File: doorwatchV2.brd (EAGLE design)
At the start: 160 x 100 mm, 40 parts, among them IC2 MAX3232CPE, K1 FINDER-43.61, Q1 IRLZ44Z, T1 BC847, T2 BC847, T3 BC847, T4 BC847, X1 MKDSN1,5/2-5,08, X2 D-SUB9-H2M09RA, X3 MKDSN1,5/2-5,08

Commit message: first rough layout of components
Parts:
- moved Q1 209.2 mm to (149.9, 63.5), turned to 90 degrees
- moved X3 198.8 mm to (154.9, 94.0), turned to 90 degrees
- moved X1 181.5 mm to (154.9, 80.0), turned to 90 degrees
- moved K1 178.9 mm to (143.5, 91.4), turned to 90 degrees
- moved T3 176.9 mm to (99.1, 72.4)
- moved R10 172.7 mm to (149.9, 81.3), turned to 270 degrees
- moved R5 163.2 mm to (83.8, 64.8), turned to 90 degrees
- moved R1 157.6 mm to (83.8, 72.4), turned to 90 degrees
- moved R7 152.6 mm to (94.0, 71.1)
- moved R3 147.9 mm to (94.0, 66.0)
- moved OK1 146.3 mm to (85.1, 69.8), turned to 270 degrees
- moved T2 134.8 mm to (64.8, 68.6), turned to 270 degrees
- moved R9 127.4 mm to (58.4, 68.6), turned to 180 degrees
- moved T1 127.1 mm to (64.8, 64.8), turned to 270 degrees
- moved R8 122.6 mm to (58.4, 66.0), turned to 180 degrees
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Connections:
- net GND: now also LED4.C; no longer R11.2
- net N$28: now also R11.1; no longer LED4.A
- net N$29: now also LED4.A, R11.2; no longer LED4.C, R11.1

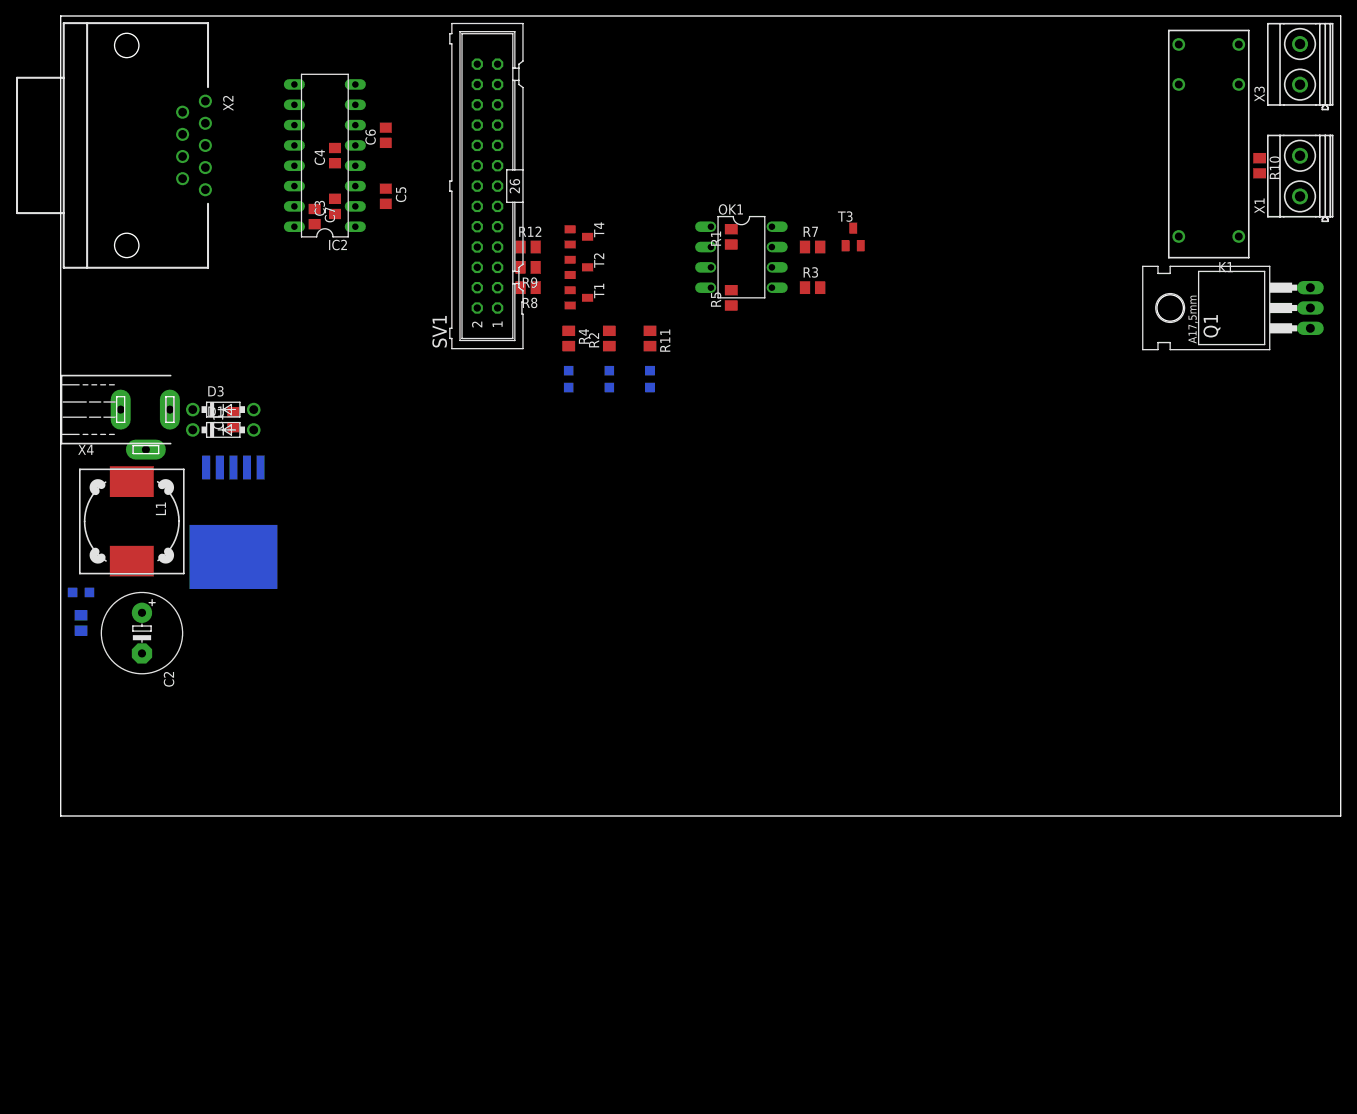
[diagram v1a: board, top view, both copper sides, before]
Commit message: added mounting-holes to schematic
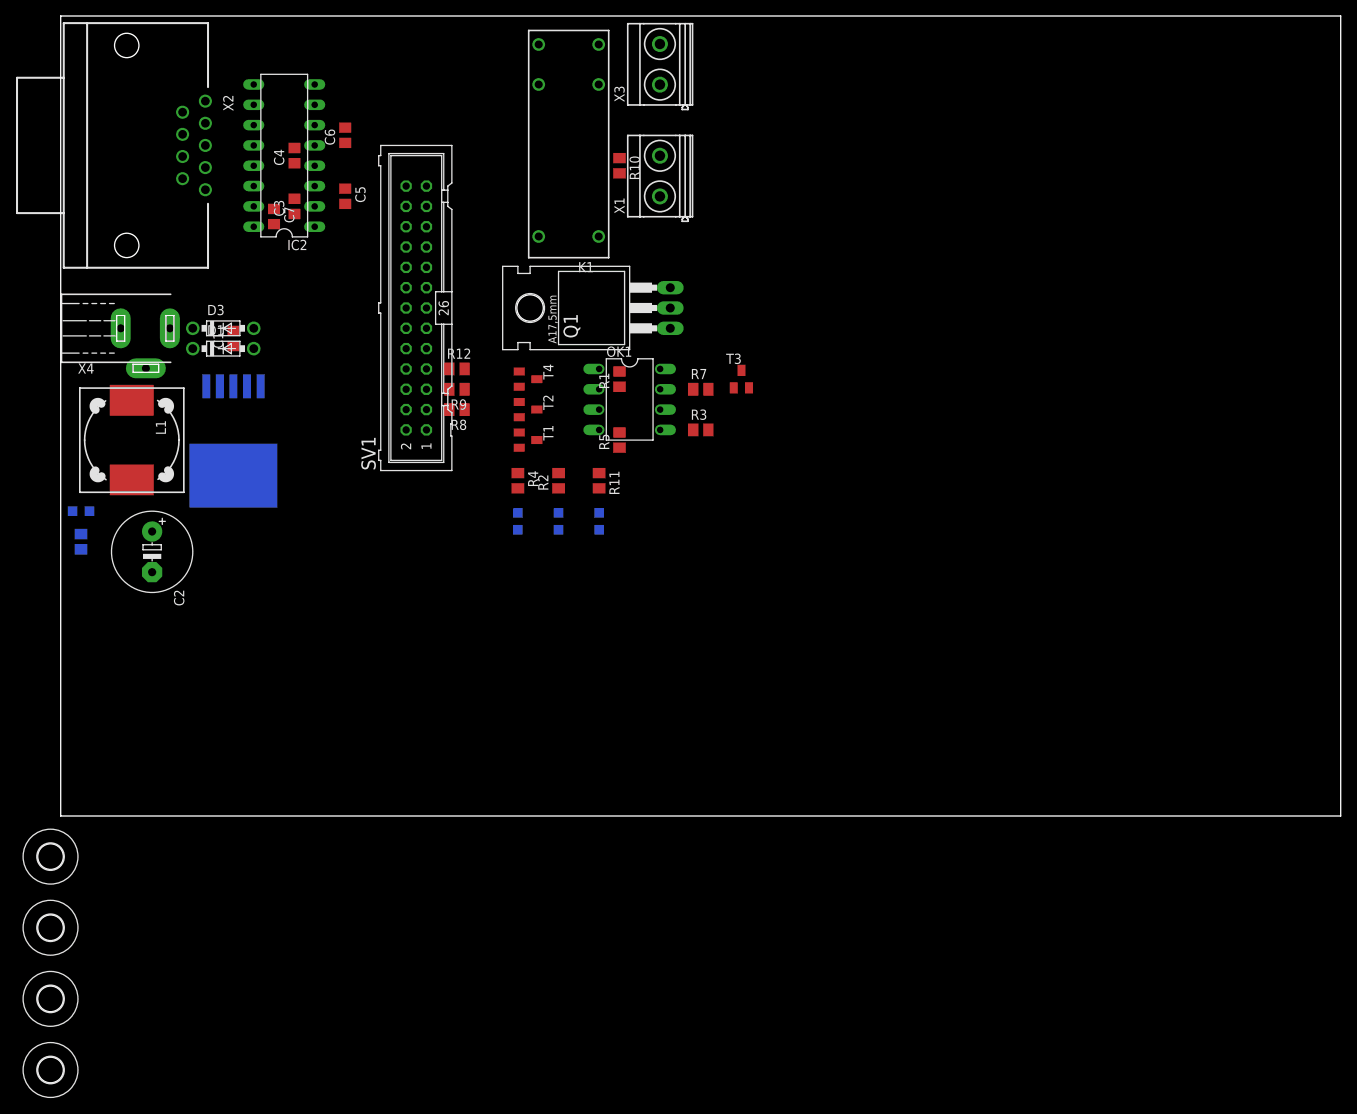
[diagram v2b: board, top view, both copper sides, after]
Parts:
- added H1, H2, H3, H4: MOUNT-HOLE3.2, holes:3,2
- moved Q1 80.0 mm to (69.8, 63.5)
- moved R10 80.0 mm to (69.8, 81.3)
- moved K1 80.0 mm to (63.5, 91.4)
- moved X1 80.0 mm to (74.9, 80.0)
- moved X3 80.0 mm to (74.9, 94.0)
- moved R3 22.6 mm to (80.0, 48.3)
- moved R1 22.6 mm to (69.8, 54.6)
- moved R7 22.6 mm to (80.0, 53.3)
- moved T3 22.6 mm to (85.1, 54.6)
- moved OK1 22.6 mm to (71.1, 52.1)
- moved R5 22.6 mm to (69.8, 47.0)
- moved LED1 18.9 mm to (57.1, 36.8)
- moved LED2 18.9 mm to (62.2, 36.8)
- moved LED4 18.9 mm to (67.3, 36.8)
- moved R11 18.9 mm to (67.3, 41.9)
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
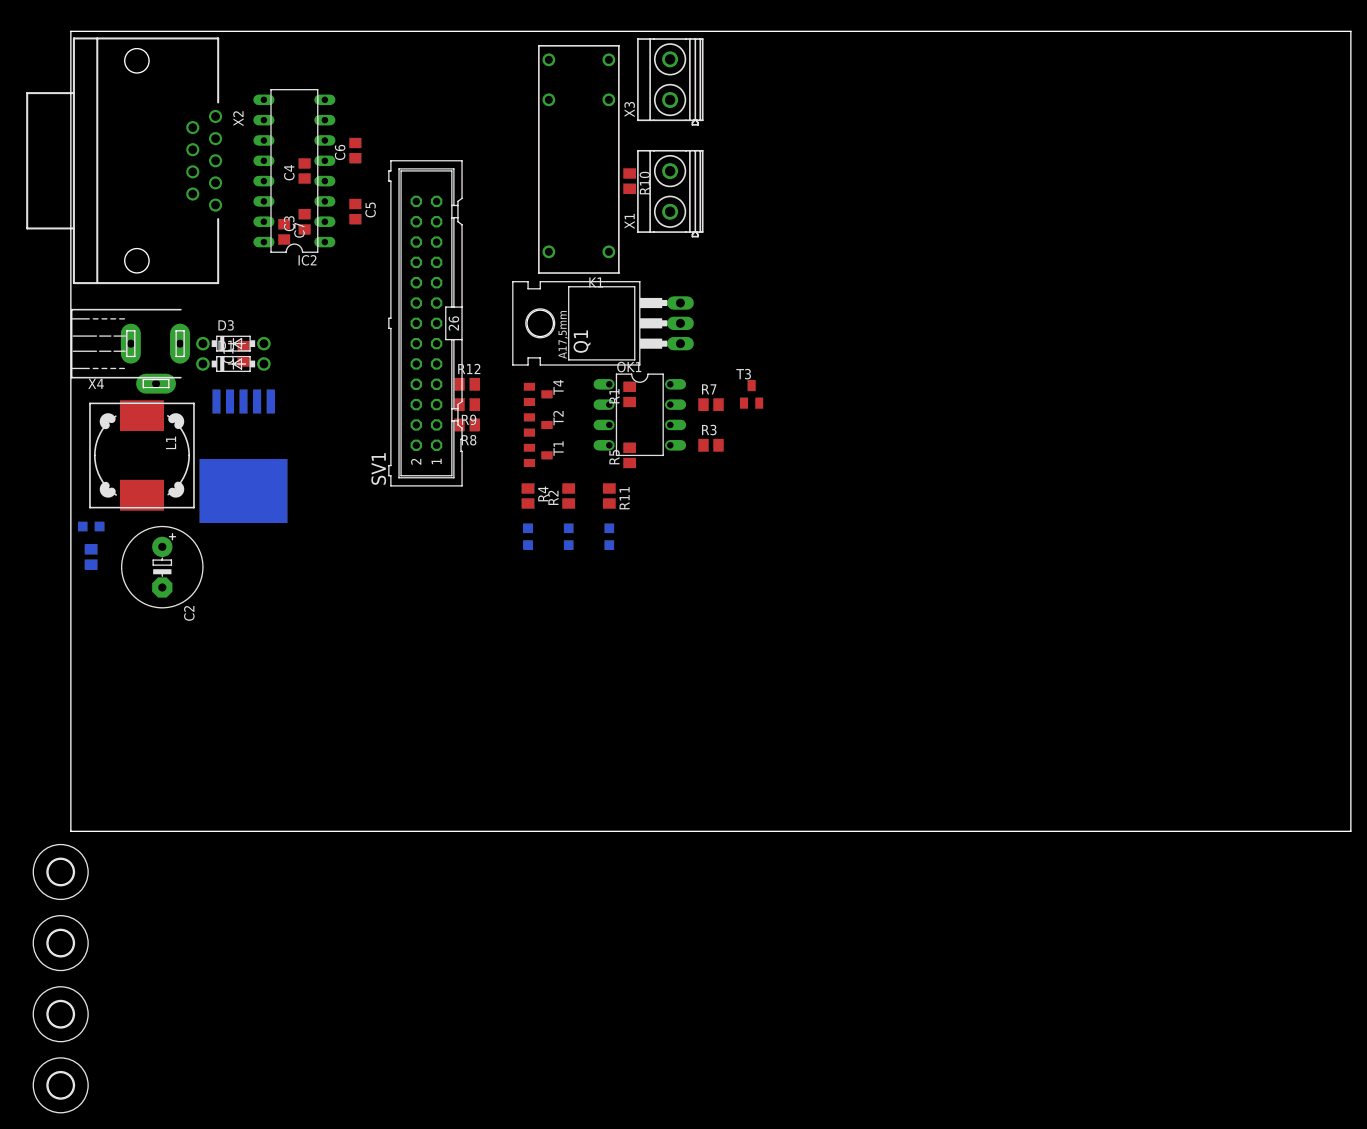
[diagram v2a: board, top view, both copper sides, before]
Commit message: first version of finished layout added white-print layers and adjusted it. adapted the trace width of higher current traces
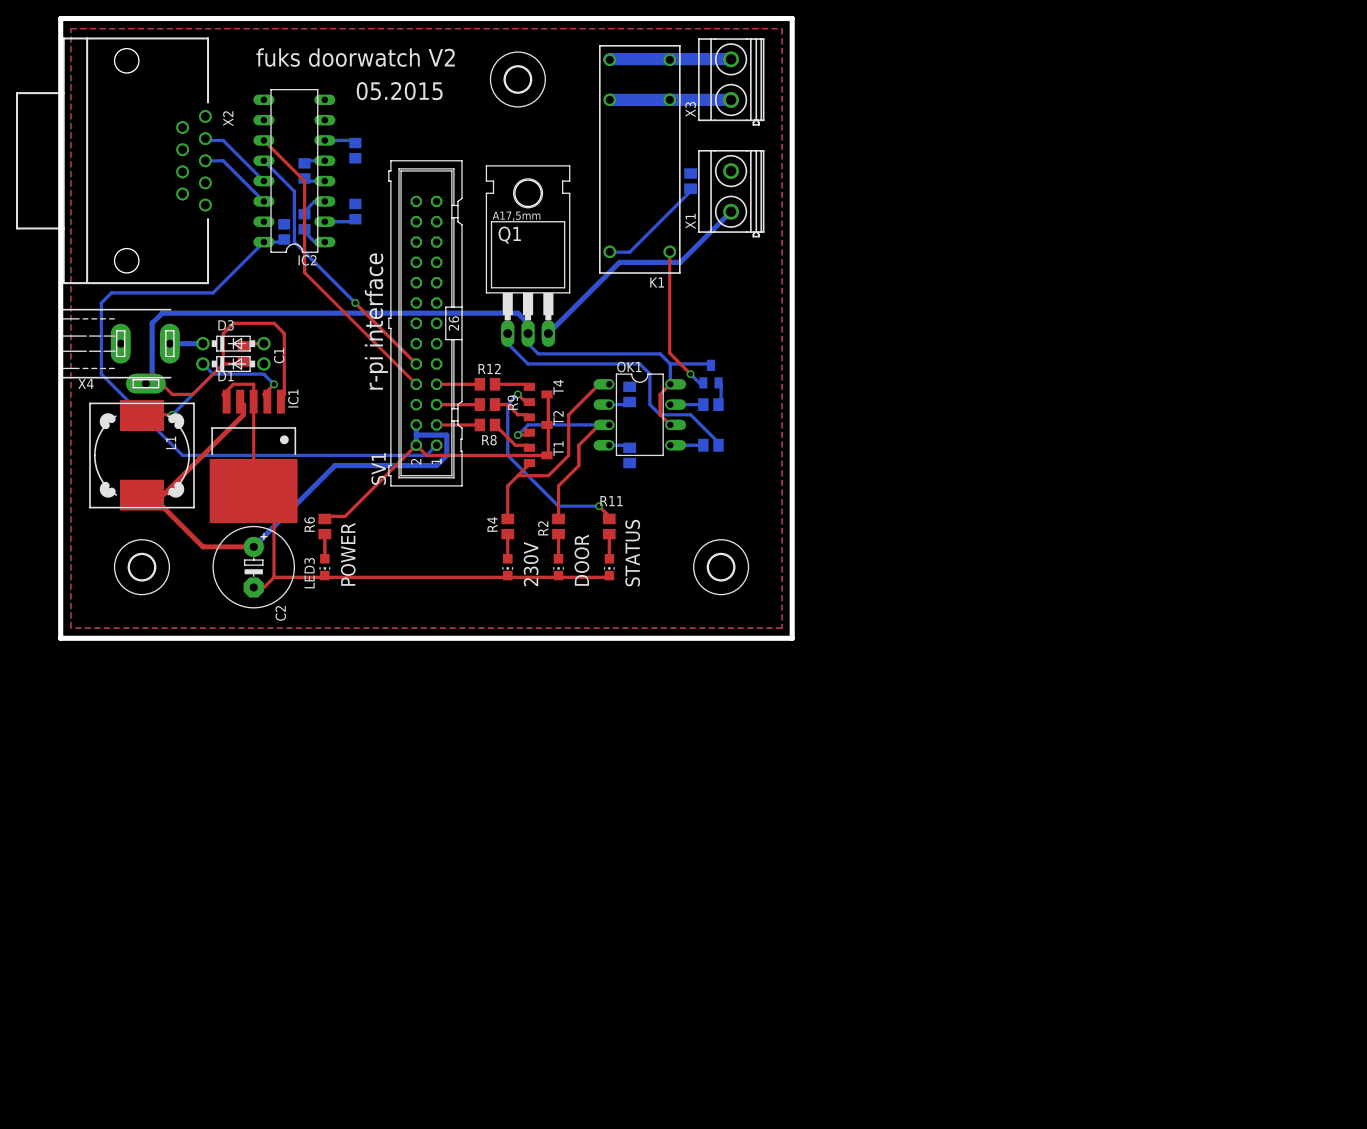
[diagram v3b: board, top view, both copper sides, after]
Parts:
- removed H4: MOUNT-HOLE3.2, holes:3,2
- IC1: value (none) -> LM2576S-5.0
- moved H2 122.1 mm to (55.9, 94.0)
- moved H3 99.7 mm to (81.3, 33.0)
- moved H1 39.4 mm to (8.89, 33.0)
- moved LED3 29.6 mm to (31.8, 33.0), flipped to the top, turned to 180 degrees
- moved R6 29.5 mm to (31.8, 38.1), flipped to the top
- moved Q1 13.7 mm to (57.1, 68.6), turned to 0 degrees
- moved C2 11.4 mm to (22.9, 33.0)
- moved K1 7.62 mm to (71.1, 91.4)
- moved R10 7.62 mm to (77.5, 81.3), flipped to the bottom
- moved X1 7.62 mm to (82.5, 80.0)
- moved X3 7.62 mm to (82.5, 94.0)
- moved T3 5.68 mm to (80.0, 57.1), flipped to the bottom
- moved LED1 4.58 mm to (54.6, 33.0), flipped to the top
- moved R4 4.58 mm to (54.6, 38.1)
- moved LED2 4.02 mm to (61.0, 33.0), flipped to the top
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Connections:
- net +5V: now also R6.1; no longer LED3.A
- net GND: now also LED3.C; no longer R6.2
- net N$18: now also LED3.A, R6.2; no longer LED3.C, R6.1
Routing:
- net +12V: track 0.00 -> 128.0 mm
- net +5V: track 0.00 -> 112.4 mm
- net +3V3: track 0.00 -> 81.9 mm
- net GND: track 0.00 -> 79.2 mm
- net TXD0: track 0.00 -> 38.4 mm
- net N$17: track 0.00 -> 35.8 mm
- net RXD0: track 0.00 -> 33.3 mm, vias 0 -> 1
- net N$13: track 0.00 -> 29.2 mm
- net N$8: track 0.00 -> 28.7 mm, vias 0 -> 1
- net N$10: track 0.00 -> 27.2 mm
- net N$28: track 0.00 -> 26.5 mm, vias 0 -> 2
- net N$3: track 0.00 -> 23.8 mm, vias 0 -> 2
- net N$25: track 0.00 -> 18.4 mm, vias 0 -> 1
- net N$23: track 0.00 -> 15.5 mm
- net N$22: track 0.00 -> 15.3 mm
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- added copper zone on layer 16, net GND
- added copper zone on layer 1, net N$30
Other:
- board size 160 x 100 mm -> 91.4 x 77.5 mm
- board text added: "05.2015"
- board text added: "230V"
- board text added: "DOOR"
- board text added: "POWER"
- board text added: "STATUS"
- board text added: "fuks doorwatch V2"
- board text added: "r-pi interface"

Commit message: fixed some DRC errors
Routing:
- net N$13: track 29.2 -> 33.7 mm
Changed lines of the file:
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@@
 <layer number="17" name="Pads" color="2" fill="1" visible="yes" active="yes"/>
 <layer number="18" name="Vias" color="2" fill="1" visible="yes" active="yes"/>
-<layer number="19" name="Unrouted" color="6" fill="1" visible="no" active="yes"/>
+<layer number="19" name="Unrouted" color="6" fill="1" visible="yes" active="yes"/>
 <layer number="20" name="Dimension" color="15" fill="1" visible="yes" active="yes"/>
 <layer number="21" name="tPlace" color="7" fill="1" visible="yes" active="yes"/>
@@
 <wire x1="59.69" y1="44.45" x2="62.23" y2="46.99" width="0.4064" layer="1"/>
 <wire x1="55.88" y1="44.45" x2="59.69" y2="44.45" width="0.4064" layer="1"/>
-<wire x1="67.31" y1="55.88" x2="66.04" y2="55.88" width="0.3048" layer="1"/>
+<wire x1="67.31" y1="55.88" x2="66.04" y2="55.88" width="0.4064" layer="1"/>
 <wire x1="66.04" y1="55.88" x2="62.23" y2="52.07" width="0.4064" layer="1"/>
 <wire x1="62.23" y1="52.07" x2="62.23" y2="46.99" width="0.4064" layer="1"/>
@@
 <contactref element="Q1" pad="S"/>
 <contactref element="X1" pad="1"/>
-<wire x1="68.58" y1="71.12" x2="59.69" y2="62.23" width="0.635" layer="16"/>
-<wire x1="76.2" y1="71.12" x2="68.58" y2="71.12" width="0.635" layer="16"/>
-<wire x1="82.55" y1="77.47" x2="76.2" y2="71.12" width="0.635" layer="16"/>
+<wire x1="68.58" y1="71.12" x2="59.69" y2="62.23" width="0" layer="19" extent="1-16"/>
+<wire x1="76.2" y1="71.12" x2="68.58" y2="71.12" width="0" layer="19" extent="1-16"/>
+<wire x1="59.69" y1="62.23" x2="76.2" y2="71.12" width="0" layer="19" extent="1-16"/>
 <wire x1="82.55" y1="77.47" x2="82.525" y2="77.4489" width="0.4064" layer="16"/>
+<wire x1="82.55" y1="77.47" x2="82.55" y2="69.85" width="0.635" layer="16"/>
+<wire x1="82.55" y1="69.85" x2="74.93" y2="62.23" width="0.635" layer="16"/>
+<wire x1="74.93" y1="62.23" x2="59.69" y2="62.23" width="0.635" layer="16"/>
 </signal>
 <signal name="N$22">
@@
 <wire x1="74.87" y1="72.44" x2="74.87" y2="59.75" width="0.4064" layer="1"/>
 <wire x1="74.87" y1="59.75" x2="77.47" y2="57.15" width="0.4064" layer="1"/>
-<via x="77.47" y="57.15" extent="1-16" drill="0.6"/>
+<via x="77.47" y="57.15" extent="1-16" drill="0.7" diameter="0.4064"/>
 <wire x1="77.47" y1="57.15" x2="78.57" y2="56.05" width="0.4064" layer="16"/>
 <wire x1="78.57" y1="56.05" x2="79.06" y2="56.05" width="0.4064" layer="16"/>
